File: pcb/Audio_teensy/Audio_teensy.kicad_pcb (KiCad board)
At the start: 2 copper layers, 1 part, among them U1 74LVC1G14

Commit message: v1.0
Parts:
- added C1: 1.0µF, Capacitor_SMD:C_0603_1608Metric, F.Cu at (129.9, 114.2)
- added C2: 100nF, Capacitor_SMD:C_0603_1608Metric, F.Cu at (159.3, 108.5)
- added C3: 100nF, Capacitor_SMD:C_0603_1608Metric, F.Cu at (162.3, 108.5)
- added C4: 150nF, Capacitor_SMD:C_0603_1608Metric, F.Cu at (163.6, 122.4)
- added C5: 1.0µF, Capacitor_SMD:C_0603_1608Metric, F.Cu at (133.9, 117.5)
- added C6: 2.2.µF, Capacitor_SMD:C_0603_1608Metric, F.Cu at (161.0, 122.4)
- added C7: 100nF, Capacitor_SMD:C_0603_1608Metric, F.Cu at (158.5, 122.4)
- added DRA1: DIN_Rail_Adapter, asl_footprints:DIN_Clip, F.Cu at (140.7, 104.8)
- added FB1: Ferrite Bead, Capacitor_SMD:C_0603_1608Metric, F.Cu at (146.7, 118.0)
- added J1: RJ45 Jack, asl_footprints:RJ45_SMD, F.Cu at (128.3, 82.5)
- added J2: Female Header, Connector_PinHeader_2.54mm:PinHeader_1x14_P2.54mm_Vertical_SMD_Pin1Left, F.Cu at (138.7, 123.7)
- added J3: Female Header, Connector_PinHeader_2.54mm:PinHeader_1x14_P2.54mm_Vertical_SMD_Pin1Left, F.Cu at (138.7, 108.5)
- added J4: Mono Audio Jack, asl_footprints:MonoJack, F.Cu at (148.6, 91.4)
- added J5: Mono Audio Jack, asl_footprints:MonoJack, F.Cu at (162.1, 91.4)
- added R1: 100Ω, Resistor_SMD:R_0603_1608Metric, F.Cu at (152.4, 119.1)
- added R2: 2.2KΩ, Resistor_SMD:R_0603_1608Metric, F.Cu at (149.4, 114.6)
- added R3: 2.2KΩ, Resistor_SMD:R_0603_1608Metric, F.Cu at (146.7, 113.8)
- added U2: AP7313, Package_TO_SOT_SMD:TSOT-23, F.Cu at (130.4, 117.5)
- added U3: SGTL5000, Package_DFN_QFN:QFN-32-1EP_5x5mm_P0.5mm_EP3.1x3.1mm, F.Cu at (160.8, 116.1)
- U1: value 74LVC1G14 -> Teensy3.2_smd; footprint Package_TO_SOT_SMD:TSOT-23-5 -> asl_footprints:Teensy30_31_32_LC_SMD
- moved U1 178.1 mm to (138.7, 116.1)
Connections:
- U1 pad 1: (no net) -> GND
- U1 pad 2: (no net) -> Net-(J1-Pad1)
- U1 pad 3: (no net) -> Net-(J1-Pad4)
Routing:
- net /3.3VDC: track 0.00 -> 54.8 mm, vias 0 -> 2
- net Net-(J4-PadS): track 0.00 -> 50.3 mm, vias 0 -> 2
- net Net-(J4-PadT): track 0.00 -> 49.9 mm, vias 0 -> 2
- net Net-(U1-Pad30): track 0.00 -> 37.9 mm
- net Net-(R2-Pad2): track 0.00 -> 30.8 mm, vias 0 -> 2
- net Net-(J1-Pad4): track 0.00 -> 29.7 mm
- net /1.8VDC: track 0.00 -> 28.9 mm
- net Net-(U1-Pad29): track 0.00 -> 28.5 mm
- net Net-(J1-Pad1): track 0.00 -> 25.9 mm
- net Net-(J5-PadT): track 0.00 -> 24.5 mm, vias 0 -> 2
- net /BCLK: track 0.00 -> 23.2 mm, vias 0 -> 2
- net Net-(C6-Pad2): track 0.00 -> 20.4 mm
- net Net-(R3-Pad2): track 0.00 -> 19.9 mm, vias 0 -> 2
- net /MCLK: track 0.00 -> 16.0 mm, vias 0 -> 2
- net /5VDC: track 0.00 -> 12.1 mm
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- added copper zone on B.Cu, net GND
- added copper zone on F.Cu, net GND
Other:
- board outline added: 47.2 x 44.5 mm
- rule pad_to_mask_clearance: 0.051 -> 0.0508
- rule trace_min: 0.2 -> 0.1524
- rule via_min_drill: 0.3 -> 0.2032
- rule via_min_size: 0.4 -> 0.4572
- board text added: "Left"
- board text added: "Right"
- board text added: "Teensy Audio Board v1.0"

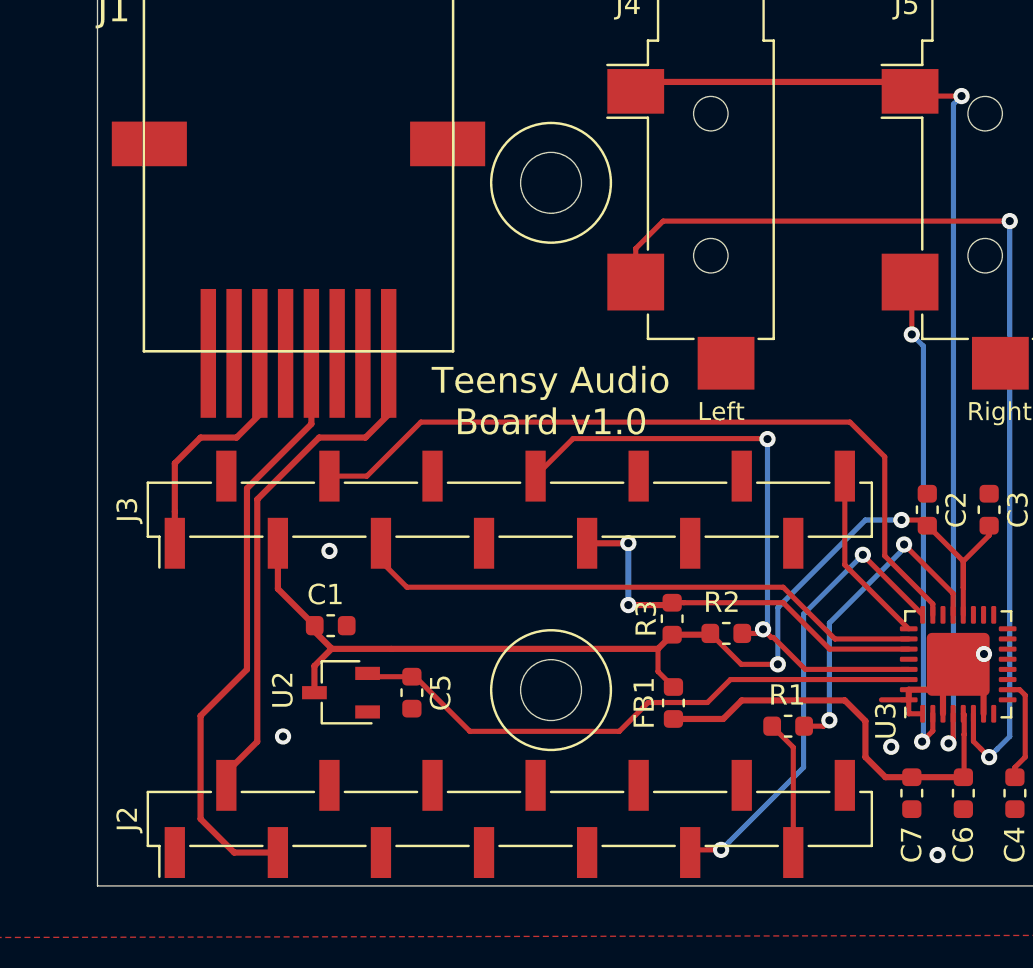
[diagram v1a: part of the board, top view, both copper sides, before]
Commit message: v1.1 AP3713 regulator pins were mapped incorrectly to footprint. Swapped Vin and GND. Added descriptions and purchase links for all components.
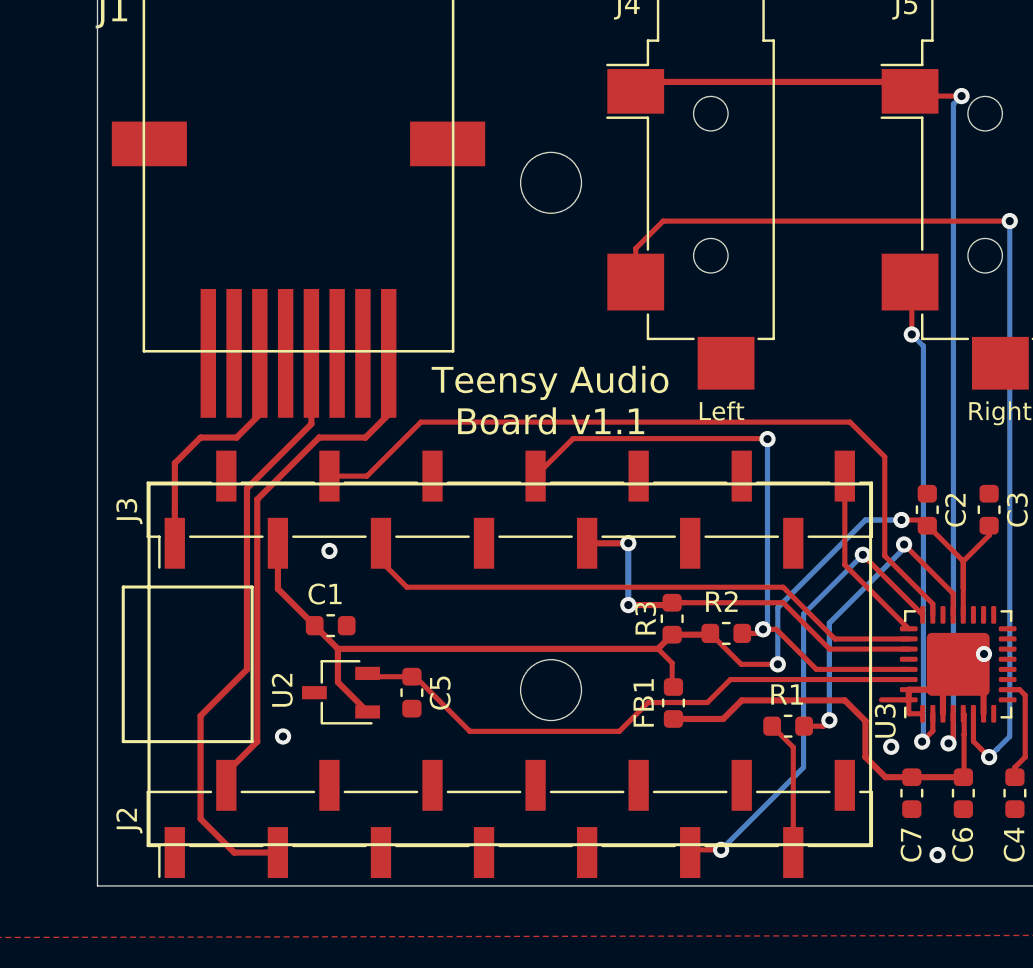
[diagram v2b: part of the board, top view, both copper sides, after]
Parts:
- C6: value 2.2.µF -> 2.2µF
- DRA1: value DIN_Rail_Adapter -> DIN Rail Adapter
- FB1: value Ferrite Bead -> 600Ω @ 100MHz
- J1: value RJ45 Jack -> 0855025008
- J2, J3: value Female Header -> SSM-114-L-SV-BE
- J4, J5: value Mono Audio Jack -> MJ-3523-SMT
- U1: value Teensy3.2_smd -> Teensy 3.2
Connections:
- U2 pad 1: GND -> /3.3VDC
- U2 pad 3: /3.3VDC -> GND
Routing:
- net /3.3VDC: track 54.8 -> 55.8 mm
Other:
- board text added: "Teensy Audio Board v1.1"
- board text removed: "Teensy Audio Board v1.0"

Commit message: upgrade to kicad 5.99
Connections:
- J1 pad 3: (no net) -> unconnected-(J1-Pad3)
- J1 pad 5: (no net) -> unconnected-(J1-Pad5)
- J1 pad 7: (no net) -> unconnected-(J1-Pad7)
- J1 pad 8: (no net) -> unconnected-(J1-Pad8)
- U1 pad 10: (no net) -> unconnected-(U1-Pad10)
- U1 pad 12: (no net) -> unconnected-(U1-Pad12)
- U1 pad 14: (no net) -> unconnected-(U1-Pad14)
- U1 pad 21: (no net) -> unconnected-(U1-Pad21)
- U1 pad 22: (no net) -> unconnected-(U1-Pad22)
- U1 pad 23: (no net) -> unconnected-(U1-Pad23)
- U1 pad 24: (no net) -> unconnected-(U1-Pad24)
- U1 pad 27: (no net) -> unconnected-(U1-Pad27)
- U1 pad 28: (no net) -> unconnected-(U1-Pad28)
- U1 pad 32: (no net) -> unconnected-(U1-Pad32)
- U1 pad 4: (no net) -> unconnected-(U1-Pad4)
- U1 pad 5: (no net) -> unconnected-(U1-Pad5)
- U1 pad 6: (no net) -> unconnected-(U1-Pad6)
- U1 pad 7: (no net) -> unconnected-(U1-Pad7)
- U1 pad 8: (no net) -> unconnected-(U1-Pad8)
- U1 pad 9: (no net) -> unconnected-(U1-Pad9)
- U3 pad 11: (no net) -> unconnected-(U3-Pad11)
- U3 pad 12: (no net) -> unconnected-(U3-Pad12)
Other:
- net class Default removed
- board text added: "Teensy Audio Board v1.2"
- board text removed: "Teensy Audio Board v1.1"
